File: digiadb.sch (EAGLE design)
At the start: 3 parts

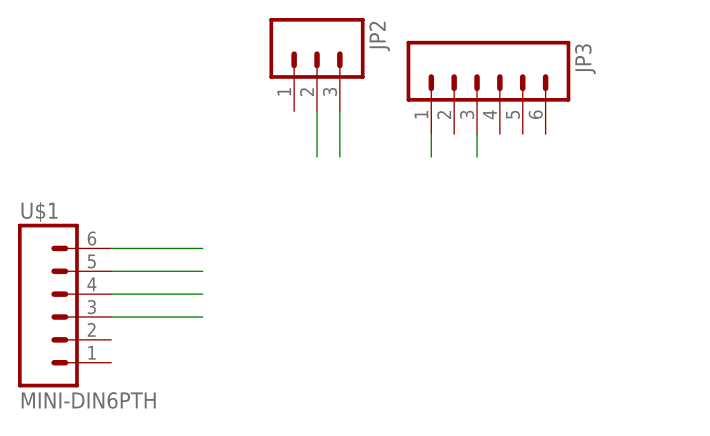
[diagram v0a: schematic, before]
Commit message: added missing 470Ω pullup resistor from adb
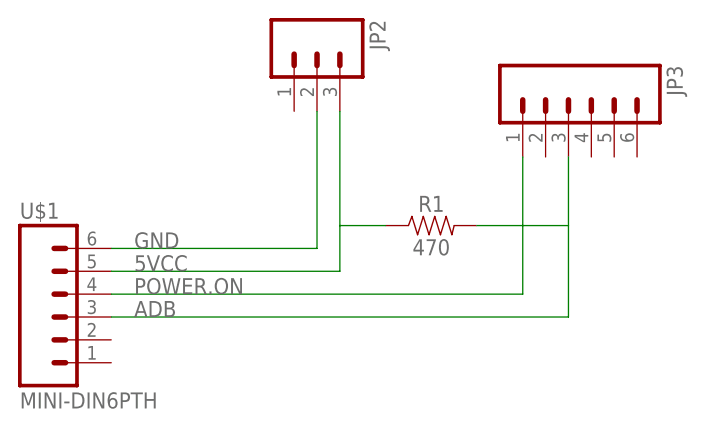
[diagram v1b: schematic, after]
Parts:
- added R1: 470, SparkFun-Resistors:470OHM-0603-1/10W-1%
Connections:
- net GND1 renamed GND
- net 5VCC: now also R1.1
- net ADB: now also R1.2
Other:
- moved on the sheet: JP3
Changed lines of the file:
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@@
 <?xml version="1.0" encoding="utf-8"?>
 <!DOCTYPE eagle SYSTEM "eagle.dtd">
-<eagle version="7.2.0">
+<eagle version="9.0.1">
 <drawing>
 <settings>
-<setting alwaysvectorfont="no"/>
+<setting alwaysvectorfont="yes"/>
+<setting keepoldvectorfont="yes"/>
 <setting verticaltext="up"/>
 </settings>
@@
 <layers>
 <layer number="1" name="Top" color="4" fill="1" visible="no" active="no"/>
+<layer number="2" name="Route2" color="1" fill="3" visible="no" active="no"/>
+<layer number="3" name="Route3" color="4" fill="3" visible="no" active="no"/>
+<layer number="4" name="Route4" color="1" fill="4" visible="no" active="no"/>
+<layer number="5" name="Route5" color="4" fill="4" visible="no" active="no"/>
+<layer number="6" name="Route6" color="1" fill="8" visible="no" active="no"/>
+<layer number="7" name="Route7" color="4" fill="8" visible="no" active="no"/>
+<layer number="8" name="Route8" color="1" fill="2" visible="no" active="no"/>
+<layer number="9" name="Route9" color="4" fill="2" visible="no" active="no"/>
+<layer number="10" name="Route10" color="1" fill="7" visible="no" active="no"/>
+<layer number="11" name="Route11" color="4" fill="7" visible="no" active="no"/>
+<layer number="12" name="Route12" color="1" fill="5" visible="no" active="no"/>
+<layer number="13" name="Route13" color="4" fill="5" visible="no" active="no"/>
+<layer number="14" name="Route14" color="1" fill="6" visible="no" active="no"/>
+<layer number="15" name="Route15" color="4" fill="6" visible="no" active="no"/>
 <layer number="16" name="Bottom" color="1" fill="1" visible="no" active="no"/>
 <layer number="17" name="Pads" color="2" fill="1" visible="no" active="no"/>
@@
 <part name="JP3" library="SparkFun" deviceset="M06" device="SIP"/>
 <part name="U$1" library="SparkFun-Connectors" deviceset="MINI-DIN6" device="PTH"/>
+<part name="R1" library="SparkFun-Resistors" library_urn="urn:adsk.eagle:library:532" deviceset="470OHM" device="-0603-1/10W-1%" package3d_urn="urn:adsk.eagle:package:39650/1" value="470"/>
 </parts>
 <sheets>
@@
 <instances>
 <instance part="JP2" gate="G$1" x="66.04" y="86.36" rot="R270"/>
-<instance part="JP3" gate="G$1" x="83.82" y="81.28" rot="R270"/>
+<instance part="JP3" gate="G$1" x="93.98" y="78.74" rot="R270"/>
 <instance part="U$1" gate="G$1" x="38.1" y="55.88"/>
+<instance part="R1" gate="G$1" x="78.74" y="66.04"/>
 </instances>
 <busses>
 </busses>
 <nets>
-<net name="GND1" class="0">
+<net name="GND" class="0">
 <segment>
 <pinref part="U$1" gate="G$1" pin="6"/>
-<wire x1="43.18" y1="63.5" x2="53.34" y2="63.5" width="0.1524" layer="91"/>
-</segment>
-<segment>
+<label x="45.72" y="63.5" size="1.778" layer="95"/>
 <pinref part="JP2" gate="G$1" pin="2"/>
-<wire x1="66.04" y1="78.74" x2="66.04" y2="73.66" width="0.1524" layer="91"/>
+<wire x1="43.18" y1="63.5" x2="66.04" y2="63.5" width="0.1524" layer="91"/>
+<wire x1="66.04" y1="63.5" x2="66.04" y2="78.74" width="0.1524" layer="91"/>
 </segment>
 </net>
@@
 <segment>
 <pinref part="U$1" gate="G$1" pin="5"/>
-<wire x1="43.18" y1="60.96" x2="53.34" y2="60.96" width="0.1524" layer="91"/>
-</segment>
-<segment>
+<label x="45.72" y="60.96" size="1.778" layer="95"/>
+<wire x1="43.18" y1="60.96" x2="68.58" y2="60.96" width="0.1524" layer="91"/>
 <pinref part="JP2" gate="G$1" pin="3"/>
-<wire x1="68.58" y1="78.74" x2="68.58" y2="73.66" width="0.1524" layer="91"/>
+<wire x1="68.58" y1="60.96" x2="68.58" y2="66.04" width="0.1524" layer="91"/>
+<pinref part="R1" gate="G$1" pin="1"/>
+<wire x1="68.58" y1="66.04" x2="68.58" y2="78.74" width="0.1524" layer="91"/>
+<wire x1="73.66" y1="66.04" x2="68.58" y2="66.04" width="0.1524" layer="91"/>
 </segment>
 </net>
@@
 <segment>
 <pinref part="U$1" gate="G$1" pin="4"/>
-<wire x1="43.18" y1="58.42" x2="53.34" y2="58.42" width="0.1524" layer="91"/>
-</segment>
-<segment>
+<label x="45.72" y="58.42" size="1.778" layer="95"/>
+<wire x1="43.18" y1="58.42" x2="88.9" y2="58.42" width="0.1524" layer="91"/>
 <pinref part="JP3" gate="G$1" pin="1"/>
-<wire x1="78.74" y1="76.2" x2="78.74" y2="73.66" width="0.1524" layer="91"/>
+<wire x1="88.9" y1="58.42" x2="88.9" y2="73.66" width="0.1524" layer="91"/>
 </segment>
 </net>
@@
 <segment>
 <pinref part="U$1" gate="G$1" pin="3"/>
-<wire x1="43.18" y1="55.88" x2="53.34" y2="55.88" width="0.1524" layer="91"/>
-</segment>
-<segment>
+<label x="45.72" y="55.88" size="1.778" layer="95"/>
+<wire x1="43.18" y1="55.88" x2="93.98" y2="55.88" width="0.1524" layer="91"/>
 <pinref part="JP3" gate="G$1" pin="3"/>
-<wire x1="83.82" y1="76.2" x2="83.82" y2="73.66" width="0.1524" layer="91"/>
+<wire x1="93.98" y1="55.88" x2="93.98" y2="66.04" width="0.1524" layer="91"/>
+<pinref part="R1" gate="G$1" pin="2"/>
+<wire x1="93.98" y1="66.04" x2="93.98" y2="73.66" width="0.1524" layer="91"/>
+<wire x1="83.82" y1="66.04" x2="93.98" y2="66.04" width="0.1524" layer="91"/>
 </segment>
 </net>
@@
 </schematic>
 </drawing>
+<compatibility>
+<note version="8.2" severity="warning">
+Since Version 8.2, EAGLE supports online libraries. The ids
+of those online libraries will not be understood (or retained)
+with this version.
+</note>
+<note version="8.3" severity="warning">
+Since Version 8.3, EAGLE supports URNs for individual library
+assets (packages, symbols, and devices). The URNs of those assets
+will not be understood (or retained) with this version.
+</note>
+<note version="8.3" severity="warning">
+Since Version 8.3, EAGLE supports the association of 3D packages
+with devices in libraries, schematics, and board files. Those 3D
+packages will not be understood (or retained) with this version.
+</note>
+</compatibility>
 </eagle>
